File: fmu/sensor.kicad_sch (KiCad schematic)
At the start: 9 parts, among them U3 BNO055, U8 AR0130CSSC00SPBA0-DR

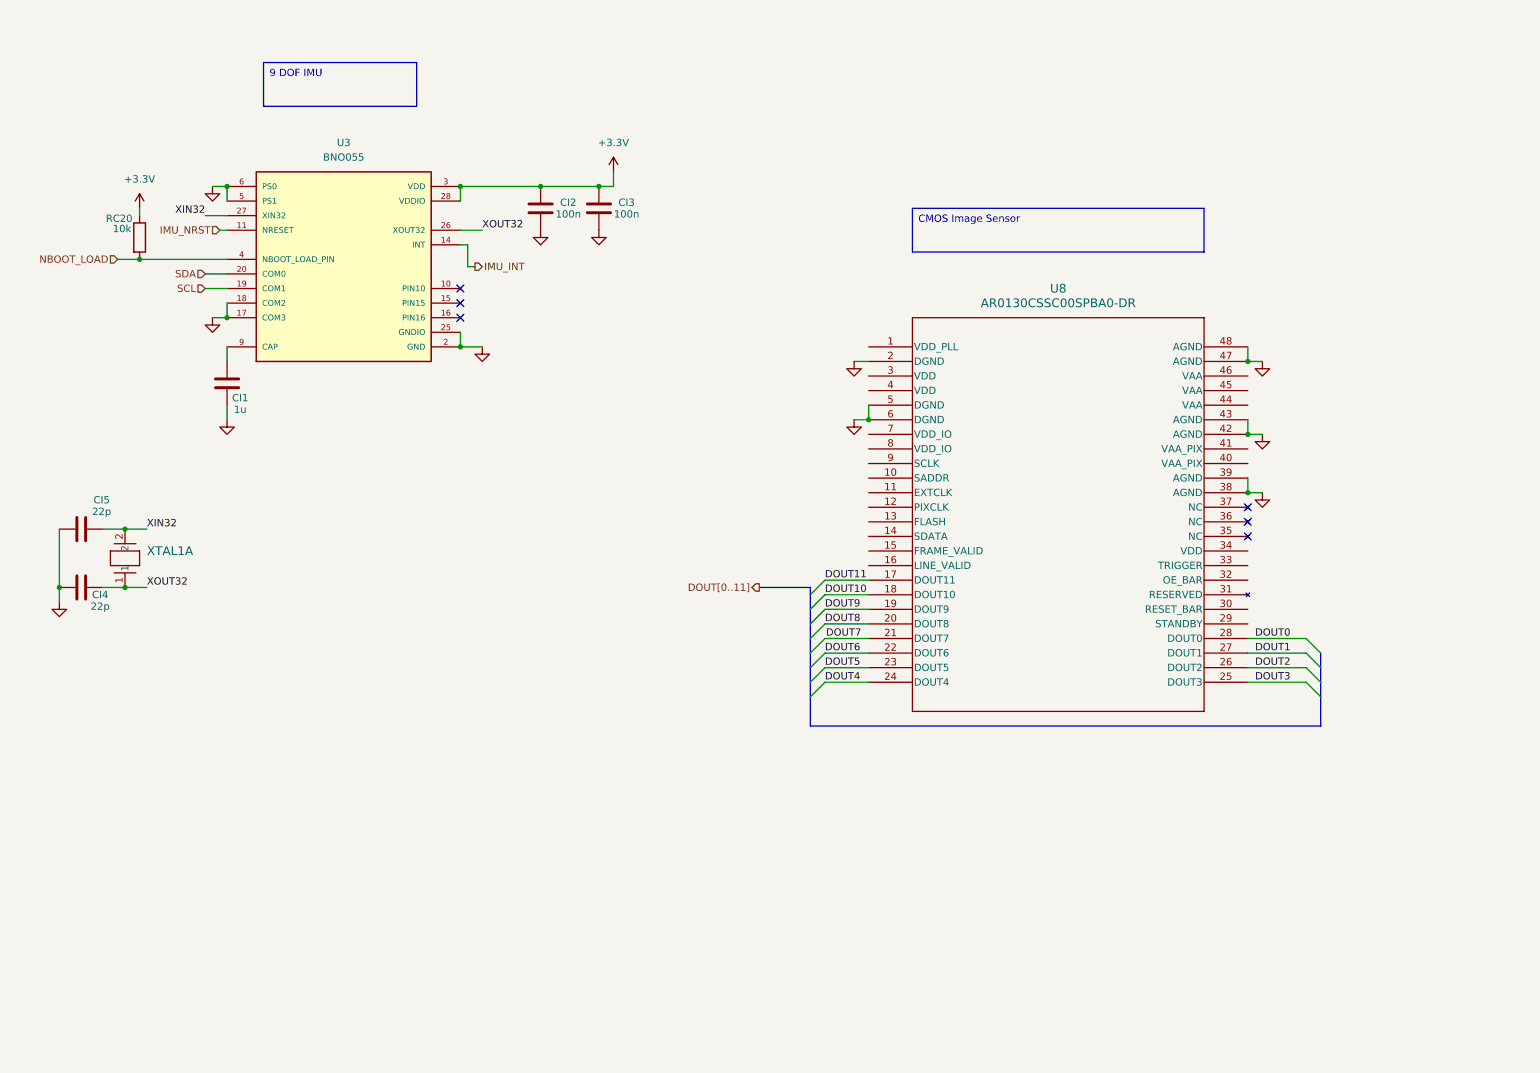
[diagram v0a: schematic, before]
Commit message: Connect motors and MCU
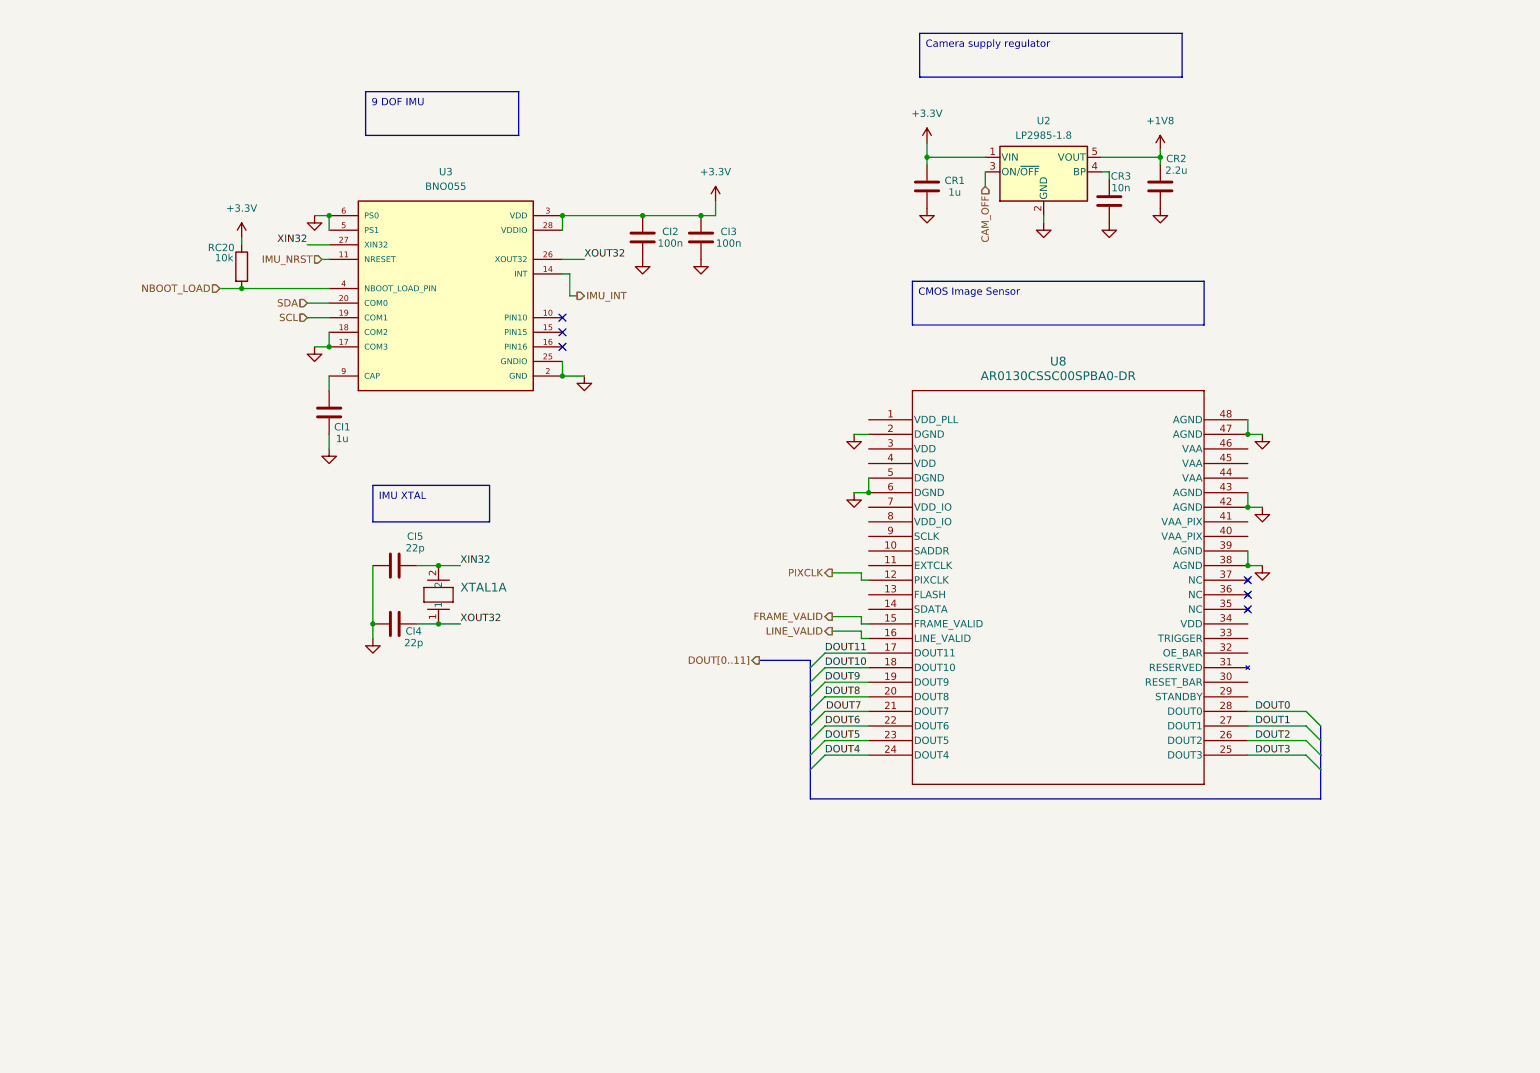
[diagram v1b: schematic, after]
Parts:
- added CR1: 1u, Capacitor_SMD:C_0603_1608Metric, symbol Device:C
- added CR2: 2.2u, Capacitor_SMD:C_0603_1608Metric, symbol Device:C
- added CR3: 10n, Capacitor_SMD:C_0603_1608Metric, symbol Device:C
- added U2: LP2985-1.8, Package_TO_SOT_SMD:SOT-23-5, symbol Regulator_Linear:LP2985-1.8
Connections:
- net +3.3V: now also CR1.2, U2.1 (VIN)
- net GND: now also CR1.1, CR2.1, CR3.1, U2.2 (GND)
- net PIXCLK: now reaches U8.12 (PIXCLK)
- net FRAME_VALID: now reaches U8.15 (FRAME_VALID)
- net LINE_VALID: now reaches U8.16 (LINE_VALID)
- new net: CR3.2, U2.4 (BP)
- new net +1V8: CR2.2, U2.5 (VOUT)
- new net CAM_OFF: U2.3 (ON/~{OFF})
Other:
- moved on the sheet: CI1, CI2, CI3, CI4, CI5, RC20, U3, U8, XTAL1A

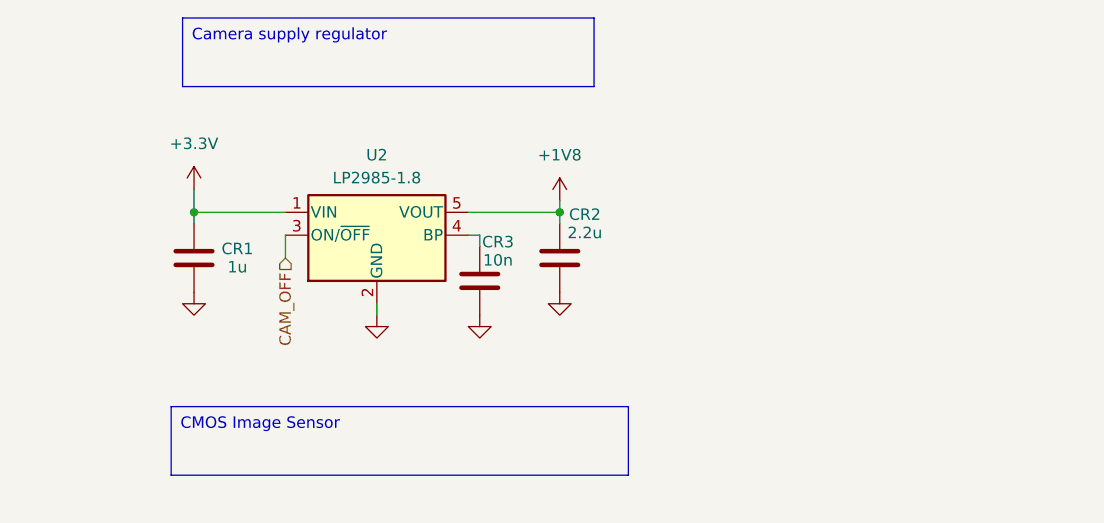
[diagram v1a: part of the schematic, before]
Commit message: Add voltage regulators
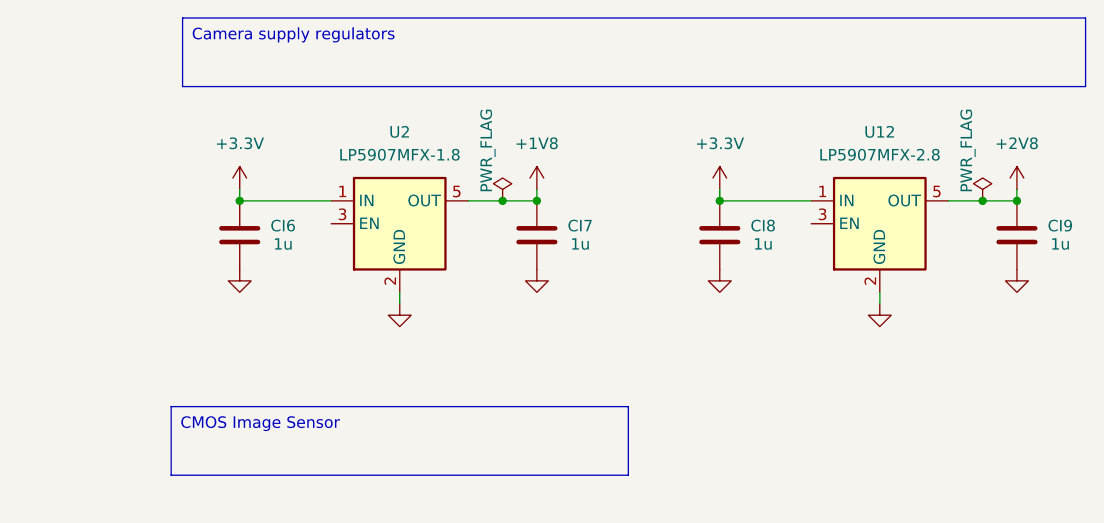
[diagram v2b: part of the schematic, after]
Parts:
- removed CR1: 1u, Capacitor_SMD:C_0603_1608Metric, symbol Device:C
- removed CR2: 2.2u, Capacitor_SMD:C_0603_1608Metric, symbol Device:C
- removed CR3: 10n, Capacitor_SMD:C_0603_1608Metric, symbol Device:C
- removed U2: LP2985-1.8, Package_TO_SOT_SMD:SOT-23-5, symbol Regulator_Linear:LP2985-1.8
- added CI6, CI7, CI8, CI9: 1u, Capacitor_SMD:C_0603_1608Metric, symbol Device:C
- added U12: LP5907MFX-2.8, Package_TO_SOT_SMD:SOT-23-5, symbol Regulator_Linear:LP5907MFX-2.8
- added U2: LP5907MFX-1.8, Package_TO_SOT_SMD:SOT-23-5, symbol Regulator_Linear:LP5907MFX-1.8
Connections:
- net +1V8: now also CI7.2, U2.5 (OUT)
- net +3.3V: now also CI6.2, CI8.2, U12.1 (IN), U2.1 (IN)
- net GND: now also CI6.1, CI7.1, CI8.1, CI9.1, U12.2 (GND), U2.2 (GND)
- new net +2V8: CI9.2, U12.5 (OUT)

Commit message: Fix some connections
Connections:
- net +1V8: now also U8.3 (VDD), U8.34 (VDD), U8.4 (VDD), U8.7 (VDD_IO), U8.8 (VDD_IO)
- net +2V8: now also U8.1 (VDD_PLL), U8.40 (VAA_PIX), U8.41 (VAA_PIX), U8.44 (VAA), U8.45 (VAA), U8.46 (VAA)
- net TRIGGER: now reaches U8.33 (TRIGGER)

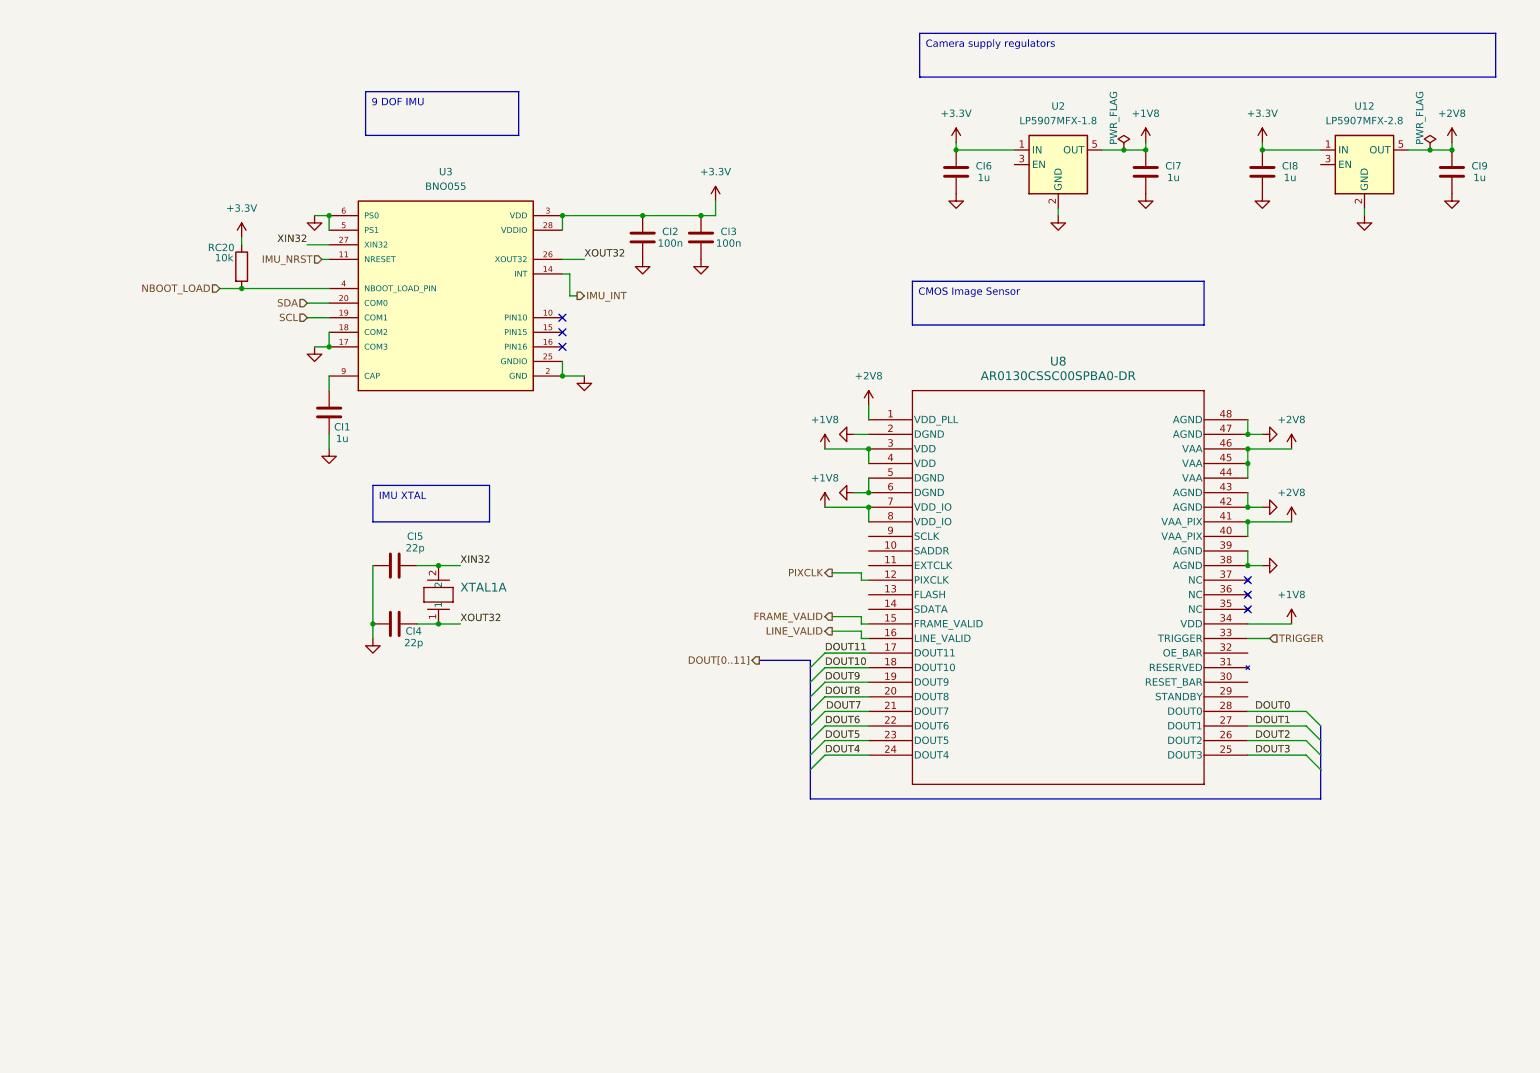
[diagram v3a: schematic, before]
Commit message: Add SD Card reader
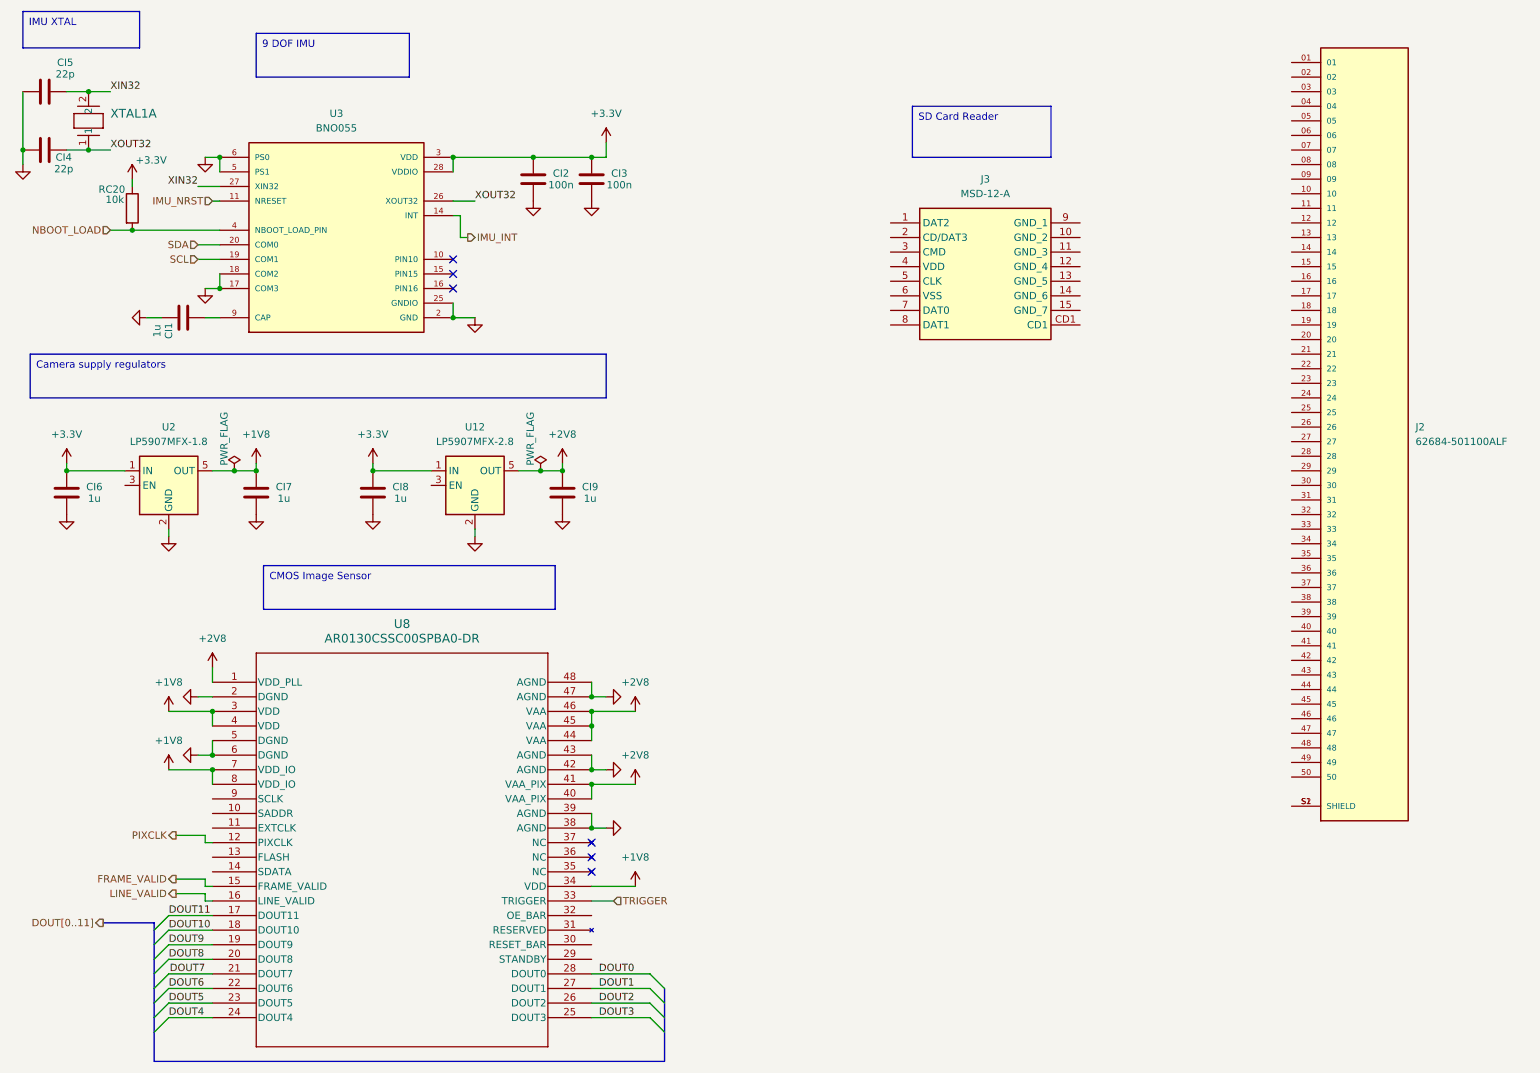
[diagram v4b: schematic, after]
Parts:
- added J2: 62684-501100ALF, 62684-501100ALF:AMPHENOL_62684-501100ALF, symbol 62684-501100ALF:62684-501100ALF
- added J3: MSD-12-A, MSD12A, symbol MSD-12-A:MSD-12-A
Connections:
- new net: J2.S1 (SHIELD), J2.S2 (SHIELD)
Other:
- moved on the sheet: CI1, CI2, CI3, CI4, CI5, CI6, CI7, CI8, CI9, RC20, U12, U2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
